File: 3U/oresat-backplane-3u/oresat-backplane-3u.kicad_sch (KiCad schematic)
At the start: 59 parts, among them J1 m55-6001642

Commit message: Added latest DXF drawing from the structure team, updated the stackup with OreSat standards, updated the page sizes, etc.
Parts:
- removed CF17.1, CF18.1: SFM-110-X1-XXX-D-LC, oresat-connectors:J-SAMTEC-CF-SFM-110-X1-XXX-D-LC, symbol oresat-connectors:J-SAMTEC-TFM-110-01-L-D-RA
- added C1, C12, C14, C15, C16, C2, C25, C26, C27, C28, C3: 10u 25V, Capacitor_SMD:C_1206_3216Metric, symbol Device:C
- added CF12.1, CF20.1, CF22.2, CF23.2, CF24.2, CF25.2, CF26.2, CF27.2, CF28.2, CF29.2, CF30.2: SFM-120-X1-XXX-D, oresat-connectors:J-SAMTEC-SFM-120-X1-XXX-D, symbol oresat-connectors:J-SAMTEC-SFM-120-X1-XXX-D
- renumbered C18 to C10, C19 to C11, C20 to C13, C15 to C17, C14 to C18, C6 to C19, C5 to C20, C13 to C21, C4 to C22, C12 to C23, C3 to C24, C1 to C4, C2 to C5, C7 to C6, C8 to C7, C16 to C8, C17 to C9, CF2.2 to CF10.2, CF3.2 to CF11.2, CF4.2 to CF13.2, CF5.2 to CF17.2, CF6.2 to CF18.2, CF7.2 to CF19.2, CF12.2 to CF2.2, CF8.2 to CF21.2, CF13.2 to CF3.2, CF20.2 to CF31.1, CF14.2 to CF4.2, CF15.2 to CF5.2, CF16.2 to CF6.2, CF17.2 to CF7.2, CF18.2 to CF8.2, CF19.2 to CF9.2, CM4.3 to CM1.2, CM2.1 to CM1.3, CM20.2 to CM12.1, CM20.1 to CM12.2, CM20.3 to CM3.3
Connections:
- net C3-UART-RX: now also CF12.1.38, CF20.1.38, CF22.2.38, CF23.2.38, CF24.2.38, CF25.2.38, CF26.2.38, CF27.2.38, CF28.2.38, CF29.2.38, CF30.2.38
- net C3-UART-TX: now also CF12.1.37, CF20.1.37, CF22.2.37, CF23.2.37, CF24.2.37, CF25.2.37, CF26.2.37, CF27.2.37, CF28.2.37, CF29.2.37, CF30.2.37
- net CAN1_H: now also CF12.1.33, CF12.1.34, CF20.1.33, CF20.1.34, CF22.2.33, CF22.2.34, CF23.2.33, CF23.2.34, CF24.2.33, CF24.2.34, CF25.2.33, CF25.2.34, CF26.2.33, CF26.2.34, CF27.2.33, CF27.2.34, CF28.2.33, CF28.2.34, CF29.2.33, CF29.2.34, CF30.2.33, CF30.2.34
- net CAN1_L: now also CF12.1.35, CF12.1.36, CF20.1.35, CF20.1.36, CF22.2.35, CF22.2.36, CF23.2.35, CF23.2.36, CF24.2.35, CF24.2.36, CF25.2.35, CF25.2.36, CF26.2.35, CF26.2.36, CF27.2.35, CF27.2.36, CF28.2.35, CF28.2.36, CF29.2.35, CF29.2.36, CF30.2.35, CF30.2.36
- net CAN2_H: now also CF12.1.17, CF12.1.18, CF20.1.17, CF20.1.18, CF22.2.17, CF22.2.18, CF23.2.17, CF23.2.18, CF24.2.17, CF24.2.18, CF25.2.17, CF25.2.18, CF26.2.17, CF26.2.18, CF27.2.17, CF27.2.18, CF28.2.17, CF28.2.18, CF29.2.17, CF29.2.18, CF30.2.17, CF30.2.18
- net CAN2_L: now also CF12.1.19, CF12.1.20, CF20.1.19, CF20.1.20, CF22.2.19, CF22.2.20, CF23.2.19, CF23.2.20, CF24.2.19, CF24.2.20, CF25.2.19, CF25.2.20, CF26.2.19, CF26.2.20, CF27.2.19, CF27.2.20, CF28.2.19, CF28.2.20, CF29.2.19, CF29.2.20, CF30.2.19, CF30.2.20
- net GND: now also C1.2, C12.2, C14.2, C15.2, C16.2, C2.2, C25.2, C26.2, C27.2, C28.2, C3.2, CF12.1.27, CF12.1.28, CF12.1.29, CF12.1.30, CF12.1.31, CF12.1.32, CF12.1.LC1, CF12.1.LC2, CF20.1.27, CF20.1.28, CF20.1.29, CF20.1.30, CF20.1.31, CF20.1.32, CF20.1.LC1, CF20.1.LC2, CF22.2.27, CF22.2.28, CF22.2.29, CF22.2.30, CF22.2.31, CF22.2.32, CF22.2.LC1, CF22.2.LC2, CF23.2.27, CF23.2.28, CF23.2.29, CF23.2.30, CF23.2.31, CF23.2.32, CF23.2.LC1, CF23.2.LC2, CF24.2.27, CF24.2.28, CF24.2.29, CF24.2.30, CF24.2.31, CF24.2.32, CF24.2.LC1, CF24.2.LC2, CF25.2.27, CF25.2.28, CF25.2.29, CF25.2.30, CF25.2.31, CF25.2.32, CF25.2.LC1, CF25.2.LC2, CF26.2.27, CF26.2.28, CF26.2.29, CF26.2.30, CF26.2.31, CF26.2.32, CF26.2.LC1, CF26.2.LC2, CF27.2.27, CF27.2.28, CF27.2.29, CF27.2.30, CF27.2.31, CF27.2.32, CF27.2.LC1, CF27.2.LC2, CF28.2.27, CF28.2.28, CF28.2.29, CF28.2.30, CF28.2.31, CF28.2.32, CF28.2.LC1, CF28.2.LC2, CF29.2.27, CF29.2.28, CF29.2.29, CF29.2.30, CF29.2.31, CF29.2.32, CF29.2.LC1, CF29.2.LC2, CF30.2.27, CF30.2.28, CF30.2.29, CF30.2.30, CF30.2.31, CF30.2.32, CF30.2.LC1, CF30.2.LC2
- net HELICAL-DEPLOY: now also CF12.1.7, CF12.1.8, CF20.1.7, CF20.1.8, CF22.2.7, CF22.2.8, CF23.2.7, CF23.2.8, CF24.2.7, CF24.2.8, CF25.2.7, CF25.2.8, CF26.2.7, CF26.2.8, CF27.2.7, CF27.2.8, CF28.2.7, CF28.2.8, CF29.2.7, CF29.2.8, CF30.2.7, CF30.2.8
- net MAG-POWER: now also CF12.1.5, CF12.1.6, CF20.1.5, CF20.1.6, CF22.2.5, CF22.2.6, CF23.2.5, CF23.2.6, CF24.2.5, CF24.2.6, CF25.2.5, CF25.2.6, CF26.2.5, CF26.2.6, CF27.2.5, CF27.2.6, CF28.2.5, CF28.2.6, CF29.2.5, CF29.2.6, CF30.2.5, CF30.2.6
- net MAG-SCL: now also CF12.1.3, CF12.1.4, CF20.1.3, CF20.1.4, CF22.2.3, CF22.2.4, CF23.2.3, CF23.2.4, CF24.2.3, CF24.2.4, CF25.2.3, CF25.2.4, CF26.2.3, CF26.2.4, CF27.2.3, CF27.2.4, CF28.2.3, CF28.2.4, CF29.2.3, CF29.2.4, CF30.2.3, CF30.2.4
- net MAG-SDA: now also CF12.1.1, CF12.1.2, CF20.1.1, CF20.1.2, CF22.2.1, CF22.2.2, CF23.2.1, CF23.2.2, CF24.2.1, CF24.2.2, CF25.2.1, CF25.2.2, CF26.2.1, CF26.2.2, CF27.2.1, CF27.2.2, CF28.2.1, CF28.2.2, CF29.2.1, CF29.2.2, CF30.2.1, CF30.2.2
- net OPD_PWR: now also CF12.1.15, CF12.1.16, CF20.1.15, CF20.1.16, CF22.2.15, CF22.2.16, CF23.2.15, CF23.2.16, CF24.2.15, CF24.2.16, CF25.2.15, CF25.2.16, CF26.2.15, CF26.2.16, CF27.2.15, CF27.2.16, CF28.2.15, CF28.2.16, CF29.2.15, CF29.2.16, CF30.2.15, CF30.2.16
- net OPD_SCL: now also CF12.1.13, CF12.1.14, CF20.1.13, CF20.1.14, CF22.2.13, CF22.2.14, CF23.2.13, CF23.2.14, CF24.2.13, CF24.2.14, CF25.2.13, CF25.2.14, CF26.2.13, CF26.2.14, CF27.2.13, CF27.2.14, CF28.2.13, CF28.2.14, CF29.2.13, CF29.2.14, CF30.2.13, CF30.2.14
- net OPD_SDA: now also CF12.1.11, CF12.1.12, CF20.1.11, CF20.1.12, CF22.2.11, CF22.2.12, CF23.2.11, CF23.2.12, CF24.2.11, CF24.2.12, CF25.2.11, CF25.2.12, CF26.2.11, CF26.2.12, CF27.2.11, CF27.2.12, CF28.2.11, CF28.2.12, CF29.2.11, CF29.2.12, CF30.2.11, CF30.2.12
- net TURNSTILE-DEPLOY: now also CF12.1.10, CF12.1.9, CF20.1.10, CF20.1.9, CF22.2.10, CF22.2.9, CF23.2.10, CF23.2.9, CF24.2.10, CF24.2.9, CF25.2.10, CF25.2.9, CF26.2.10, CF26.2.9, CF27.2.10, CF27.2.9, CF28.2.10, CF28.2.9, CF29.2.10, CF29.2.9, CF30.2.10, CF30.2.9
- net VBUS: now also C1.1, C12.1, C14.1, C15.1, C16.1, C2.1, C25.1, C26.1, C27.1, C28.1, C3.1, CF12.1.21, CF12.1.22, CF12.1.23, CF12.1.24, CF12.1.25, CF12.1.26, CF20.1.21, CF20.1.22, CF20.1.23, CF20.1.24, CF20.1.25, CF20.1.26, CF22.2.21, CF22.2.22, CF22.2.23, CF22.2.24, CF22.2.25, CF22.2.26, CF23.2.21, CF23.2.22, CF23.2.23, CF23.2.24, CF23.2.25, CF23.2.26, CF24.2.21, CF24.2.22, CF24.2.23, CF24.2.24, CF24.2.25, CF24.2.26, CF25.2.21, CF25.2.22, CF25.2.23, CF25.2.24, CF25.2.25, CF25.2.26, CF26.2.21, CF26.2.22, CF26.2.23, CF26.2.24, CF26.2.25, CF26.2.26, CF27.2.21, CF27.2.22, CF27.2.23, CF27.2.24, CF27.2.25, CF27.2.26, CF28.2.21, CF28.2.22, CF28.2.23, CF28.2.24, CF28.2.25, CF28.2.26, CF29.2.21, CF29.2.22, CF29.2.23, CF29.2.24, CF29.2.25, CF29.2.26, CF30.2.21, CF30.2.22, CF30.2.23, CF30.2.24, CF30.2.25, CF30.2.26
- net ~{SD}: now also CF12.1.39, CF12.1.40, CF20.1.39, CF20.1.40, CF22.2.39, CF22.2.40, CF23.2.39, CF23.2.40, CF24.2.39, CF24.2.40, CF25.2.39, CF25.2.40, CF26.2.39, CF26.2.40, CF27.2.39, CF27.2.40, CF28.2.39, CF28.2.40, CF29.2.39, CF29.2.40, CF30.2.39, CF30.2.40
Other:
- company: (none) -> Portland State Aerospace Society
- title: (none) -> Generic OreSat 3U Backplane
- moved on the sheet: C1.1, C1.2, C10, C11, C13, C17, C18, C19, C20, C20.1, C20.2, C21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

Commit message: Actually commit all of the files created for the scheamtic :/
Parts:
- removed C1, C10, C11, C12, C13, C14, C15, C16, C17, C18, C19, C2, C20, C21, C22, C23, C24, C25, C26, C27, C28, C3, C4, C5, C6, C7, C8, C9: 10u 25V, Capacitor_SMD:C_1206_3216Metric, symbol Device:C
- removed C1.1, C1.2, C20.1, C20.2: 1n, oresat-passives:0603-SMALL, symbol Device:C
- removed CF1.2, CF10.2, CF11.2, CF12.1, CF13.2, CF17.2, CF18.2, CF19.2, CF2.2, CF20.1, CF21.2, CF22.2, CF23.2, CF24.2, CF25.2, CF26.2, CF27.2, CF28.2, CF29.2, CF3.2, CF30.2, CF31.1, CF4.2, CF5.2, CF6.2, CF7.2, CF8.2, CF9.2: SFM-120-X1-XXX-D, oresat-connectors:J-SAMTEC-SFM-120-X1-XXX-D, symbol oresat-connectors:J-SAMTEC-SFM-120-X1-XXX-D
- removed CM1.1, CM1.2, CM1.3, CM12.1, CM12.2, CM3.2, CM3.3, CM4.2: J-MOLEX-SMPM-73300-0111X, oresat-connectors:J-MOLEX-SMPM-73300-0111X-long, symbol oresat-connectors:J-MOLEX-SMPM-73300-0111X_1
- removed J1: m55-6001642, oresat-connectors:m55-6001642, symbol oresat-connectors:m55-6001642
- removed R1.1, R1.2, R1.3, R1.4, R20.1, R20.2, R20.3, R20.4: 60.4, Resistor_SMD:R_1206_3216Metric, symbol Device:R_US
- removed R20.5, R20.6: 0, oresat-passives:0603-SMALL, symbol Device:R_US
- added H1, H10, H11, H12, H2, H3, H4, H5, H6, H7, H8, H9: MountingHole_Pad, MountingHole:MountingHole_2.2mm_M2_DIN965_Pad, symbol Mechanical:MountingHole_Pad
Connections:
- net GND: now also H1.1, H10.1, H11.1, H12.1, H2.1, H3.1, H4.1, H5.1, H6.1, H7.1, H8.1, H9.1
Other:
- added sheet Auxiliary Connectors (oresat-backplane-3u-sch-aux.kicad_sch)
- added sheet Debug Connector (oresat-backplane-3u-sch-debug.kicad_sch)
- added sheet Main Connectors 1 (oresat-backplane-3u-sch-main-1.kicad_sch)
- added sheet Main Connectors 2 (oresat-backplane-3u-sch-main-2.kicad_sch)
- added sheet Main Connectors 3 (oresat-backplane-3u-sch-main-3.kicad_sch)
- added sheet RF Connectors (oresat-backplane-3u-sch-rf.kicad_sch)
- note removed: "Aux connectors"
- note removed: "Debug Connector"
- note removed: "Use R20.5,R20.6 to bridge CAN1 and CAN2"

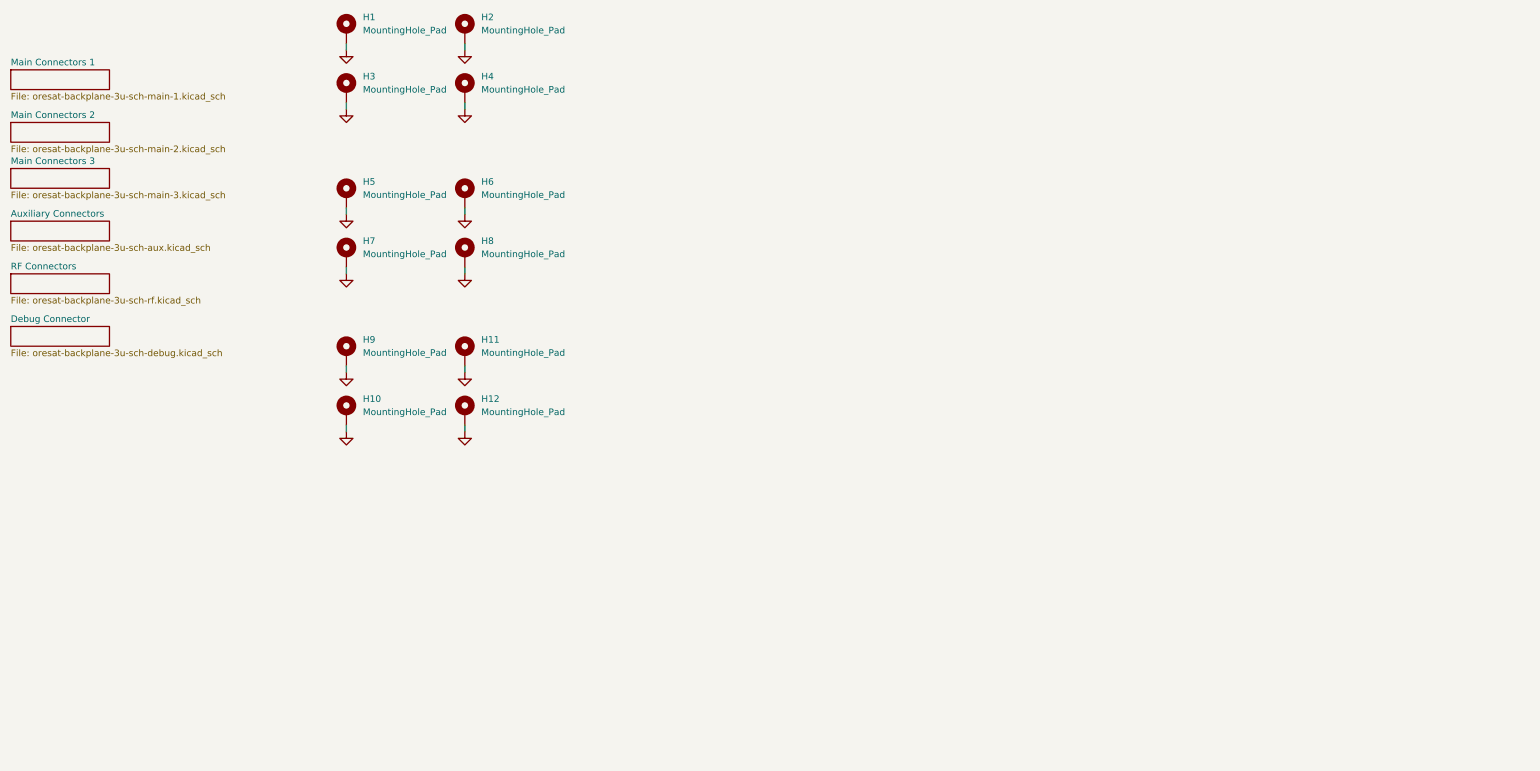
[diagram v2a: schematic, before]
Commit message: Fixed libraries and footprints, synced sch and pcb (sorry Jacob).
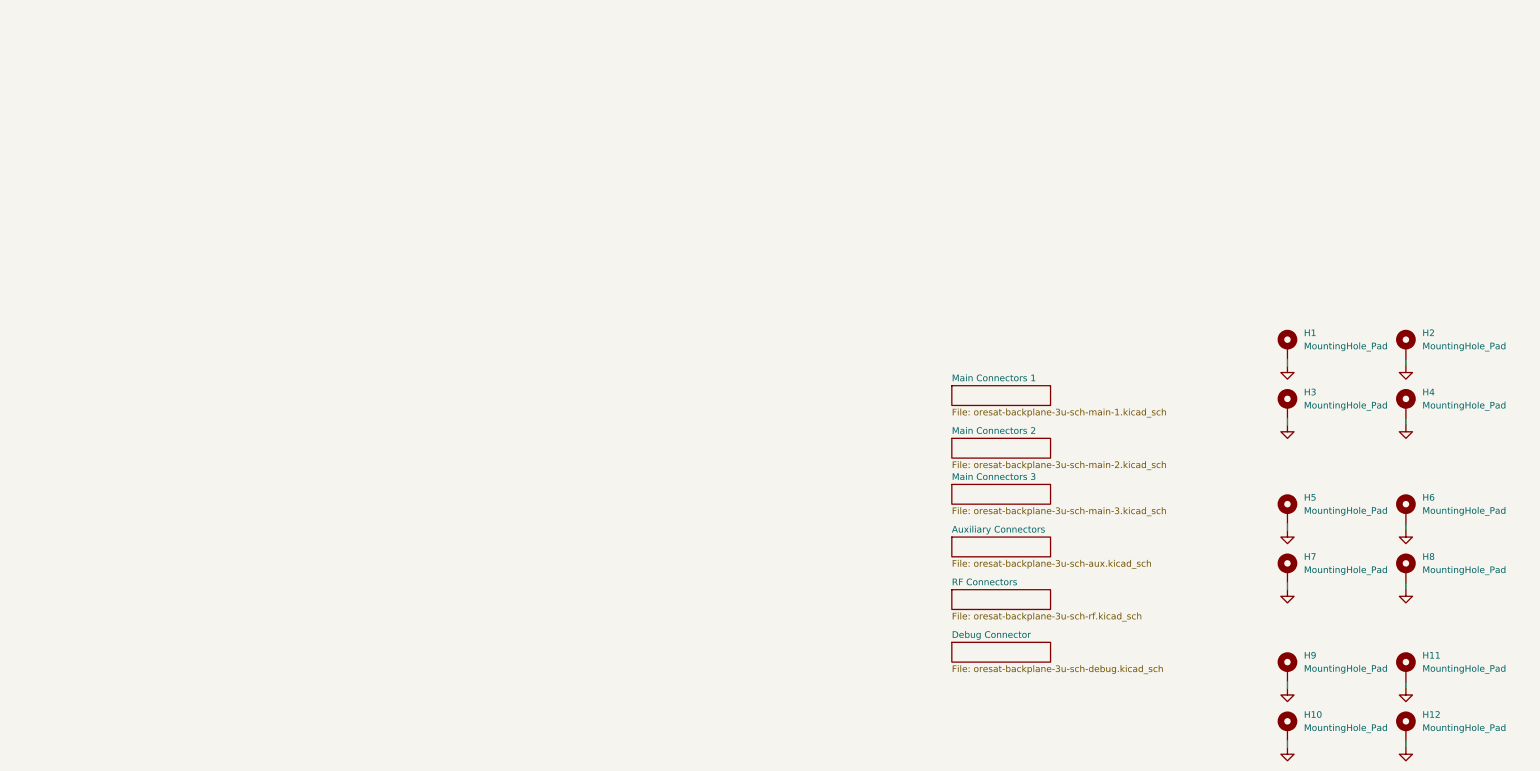
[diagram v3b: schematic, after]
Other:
- moved on the sheet: H1, H10, H11, H12, H2, H3, H4, H5, H6, H7, H8, H9

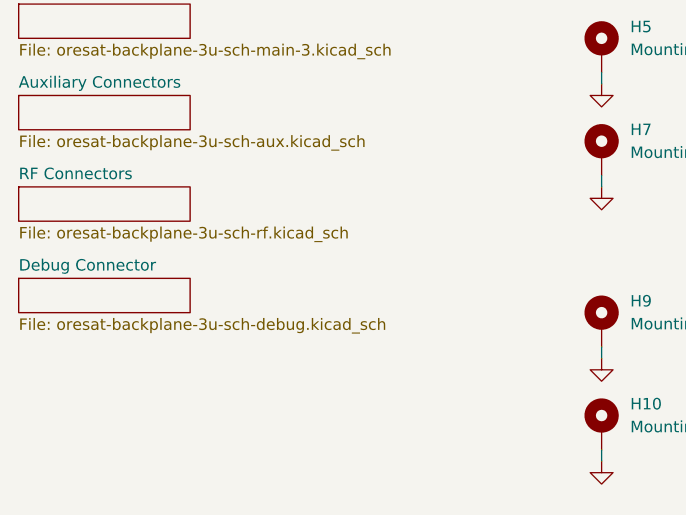
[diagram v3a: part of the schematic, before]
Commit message: Connectors laid out, unrouted
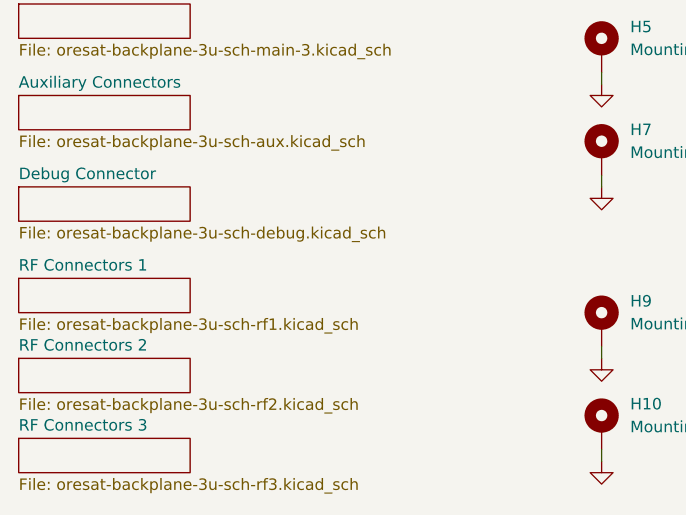
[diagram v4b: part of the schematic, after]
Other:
- removed sheet RF Connectors
- added sheet RF Connectors 1 (oresat-backplane-3u-sch-rf1.kicad_sch)
- added sheet RF Connectors 2 (oresat-backplane-3u-sch-rf2.kicad_sch)
- added sheet RF Connectors 3 (oresat-backplane-3u-sch-rf3.kicad_sch)
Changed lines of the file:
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@@
 	)
 	(sheet
-		(at 68.58 143.51)
+		(at 68.58 133.35)
 		(size 19.05 3.81)
 		(exclude_from_sim no)
@@
 		)
 		(property "Sheetname" "Debug Connector"
-			(at 68.58 142.7984 0)
+			(at 68.58 132.6384 0)
 			(effects
 				(font
@@
 		)
 		(property "Sheetfile" "oresat-backplane-3u-sch-debug.kicad_sch"
-			(at 68.58 147.9046 0)
+			(at 68.58 137.7446 0)
 			(effects
 				(font
@@
 	)
 	(sheet
+		(at 68.58 143.51)
+		(size 19.05 3.81)
+		(exclude_from_sim no)
+		(in_bom yes)
+		(on_board yes)
+		(dnp no)
+		(fields_autoplaced yes)
+		(stroke
+			(width 0.1524)
+			(type solid)
+		)
+		(fill
+			(color 0 0 0 0.0000)
+		)
+		(property "Sheetname" "RF Connectors 1"
+			(at 68.58 142.7984 0)
+			(effects
+				(font
+					(size 1.27 1.27)
+				)
+				(justify left bottom)
+			)
+		)
+		(property "Sheetfile" "oresat-backplane-3u-sch-rf1.kicad_sch"
+			(at 68.58 147.9046 0)
+			(effects
+				(font
+					(size 1.27 1.27)
+				)
+				(justify left top)
+			)
+		)
+		(property "Field2" ""
+			(at 68.58 143.51 0)
+			(effects
+				(font
+					(size 1.27 1.27)
+				)
+			)
+		)
+		(property "Field3" ""
+			(at 68.58 143.51 0)
+			(effects
+				(font
+					(size 1.27 1.27)
+				)
+			)
+		)
+		(instances
+			(project "oresat-backplane-3u"
+				(path "/300eeac4-6caf-4310-939c-5dc51539800c"
+					(page "8")
+				)
+			)
+		)
+	)
+	(sheet
 		(at 68.58 123.19)
 		(size 19.05 3.81)
@@
 	)
 	(sheet
-		(at 68.58 133.35)
-		(size 19.05 3.81)
-		(exclude_from_sim no)
-		(in_bom yes)
-		(on_board yes)
-		(dnp no)
-		(fields_autoplaced yes)
-		(stroke
-			(width 0.1524)
-			(type solid)
-		)
-		(fill
-			(color 0 0 0 0.0000)
-		)
-		(property "Sheetname" "RF Connectors"
-			(at 68.58 132.6384 0)
-			(effects
-				(font
-					(size 1.27 1.27)
-				)
-				(justify left bottom)
-			)
-		)
-		(property "Sheetfile" "oresat-backplane-3u-sch-rf.kicad_sch"
-			(at 68.58 137.7446 0)
-			(effects
-				(font
-					(size 1.27 1.27)
-				)
-				(justify left top)
-			)
-		)
-		(instances
-			(project "oresat-backplane-3u"
-				(path "/300eeac4-6caf-4310-939c-5dc51539800c"
-					(page "6")
+		(at 68.58 152.4)
+		(size 19.05 3.81)
+		(exclude_from_sim no)
+		(in_bom yes)
+		(on_board yes)
+		(dnp no)
+		(fields_autoplaced yes)
+		(stroke
+			(width 0.1524)
+			(type solid)
+		)
+		(fill
+			(color 0 0 0 0.0000)
+		)
+		(property "Sheetname" "RF Connectors 2"
+			(at 68.58 151.6884 0)
+			(effects
+				(font
+					(size 1.27 1.27)
+				)
+				(justify left bottom)
+			)
+		)
+		(property "Sheetfile" "oresat-backplane-3u-sch-rf2.kicad_sch"
+			(at 68.58 156.7946 0)
+			(effects
+				(font
+					(size 1.27 1.27)
+				)
+				(justify left top)
+			)
+		)
+		(instances
+			(project "oresat-backplane-3u"
+				(path "/300eeac4-6caf-4310-939c-5dc51539800c"
+					(page "9")
 				)
 			)
@@
 				)
 			)
+		)
+	)
+	(sheet
+		(at 68.58 161.29)
+		(size 19.05 3.81)
+		(exclude_from_sim no)
+		(in_bom yes)
+		(on_board yes)
+		(dnp no)
+		(fields_autoplaced yes)
+		(stroke
+			(width 0.1524)
+			(type solid)
+		)
+		(fill
+			(color 0 0 0 0.0000)
+		)
+		(property "Sheetname" "RF Connectors 3"
+			(at 68.58 160.5784 0)
+			(effects
+				(font
+					(size 1.27 1.27)
+				)
+				(justify left bottom)
+			)
+		)
+		(property "Sheetfile" "oresat-backplane-3u-sch-rf3.kicad_sch"
+			(at 68.58 165.6846 0)
+			(effects
+				(font
+					(size 1.27 1.27)
+				)
+				(justify left top)
+			)
+		)
+		(instances
+			(project "oresat-backplane-3u"
+				(path "/300eeac4-6caf-4310-939c-5dc51539800c"
+					(page "10")
+				)
+			)

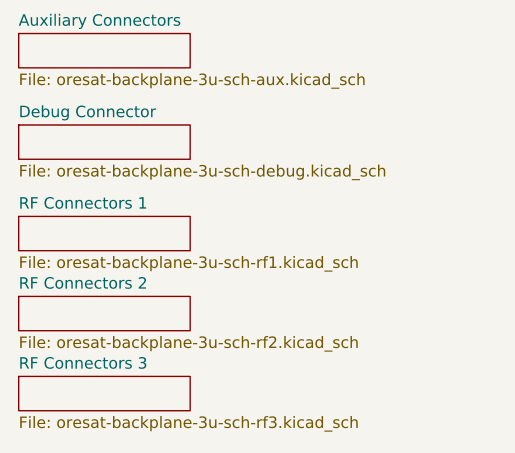
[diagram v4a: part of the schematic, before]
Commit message: Moved can lines to back & fixed RF schematic organization
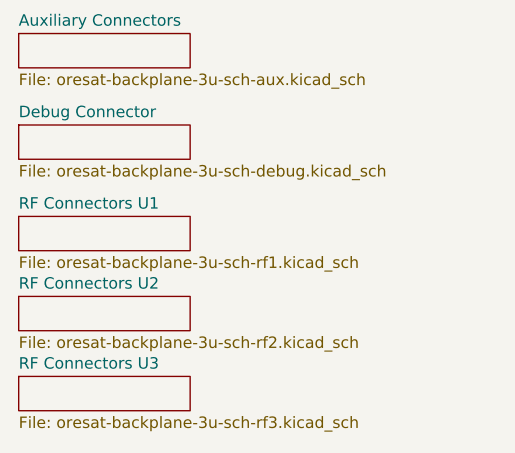
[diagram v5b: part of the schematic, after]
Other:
- sheet RF Connectors 1 renamed RF Connectors U1
- sheet RF Connectors 2 renamed RF Connectors U2
- sheet RF Connectors 3 renamed RF Connectors U3
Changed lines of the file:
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@@
 			(color 0 0 0 0.0000)
 		)
-		(property "Sheetname" "RF Connectors 1"
+		(property "Sheetname" "RF Connectors U1"
 			(at 68.58 142.7984 0)
 			(effects
@@
 			(color 0 0 0 0.0000)
 		)
-		(property "Sheetname" "RF Connectors 2"
+		(property "Sheetname" "RF Connectors U2"
 			(at 68.58 151.6884 0)
 			(effects
@@
 			(color 0 0 0 0.0000)
 		)
-		(property "Sheetname" "RF Connectors 3"
+		(property "Sheetname" "RF Connectors U3"
 			(at 68.58 160.5784 0)
 			(effects
